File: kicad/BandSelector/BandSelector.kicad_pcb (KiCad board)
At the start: 2 copper layers, 105.5 x 77.6 mm, 60 parts, among them J1 DE15_Plug_HighDensity_Mountin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, J2 POWER, J3 75915416LF, Q1 2N7000, Q2 2N7000, U1 L7805, U2 PicoW

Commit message: better, better.
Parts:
- moved Q2 28.6 mm to (138.6, 72.2), turned to 180 degrees
- moved #G1 25.1 mm to (200.0, 104.8)
- moved TP8 24.5 mm to (148.6, 89.5)
- moved TP9 24.4 mm to (146.1, 89.5)
- moved U2 24.4 mm to (149.9, 103.0)
- moved TP4 24.3 mm to (174.0, 116.8)
- moved TP5 24.3 mm to (128.3, 116.8)
- moved TP3 24.3 mm to (171.4, 116.8)
- moved TP6 24.3 mm to (125.7, 116.8)
- moved TP10 24.3 mm to (141.0, 89.5)
- moved C8 19.5 mm to (132.2, 71.1), turned to -90 degrees
- moved C4 19.4 mm to (122.4, 68.6), turned to -90 degrees
- moved L4 18.6 mm to (128.8, 57.8)
- moved L5 16.5 mm to (139.4, 68.1)
- moved C7 15.6 mm to (125.6, 65.0), turned to 90 degrees
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- renumbered G*** to #G1
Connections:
- net Net-(J1-Pad6) renamed /DIGOUT0
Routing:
- net +3.3V: track 118.8 -> 57.0 mm, vias 1 -> 0
- net Net-(Q1-D): track 0.00 -> 20.1 mm
- net /BAND0: track 22.9 -> 40.0 mm
- net Net-(Q2-G): track 26.9 -> 15.1 mm
- net /BLINKY: track 21.5 -> 32.0 mm
- net /PWRON: track 6.12 -> 16.6 mm
- net /\PWRSENSE: track 8.15 -> 16.8 mm
- net /B3: track 8.59 -> 17.2 mm
- net /\PWR_ON: track 24.5 -> 18.1 mm
- net /B2: track 8.72 -> 13.5 mm
- net Net-(D6-K): track 22.0 -> 26.3 mm
- net Net-(D9-K): track 22.0 -> 17.8 mm
- net /DIGOUT1: track 19.8 -> 16.0 mm
- net +5VD: track 76.7 -> 73.2 mm
- net Net-(D8-K): track 33.5 -> 36.9 mm
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
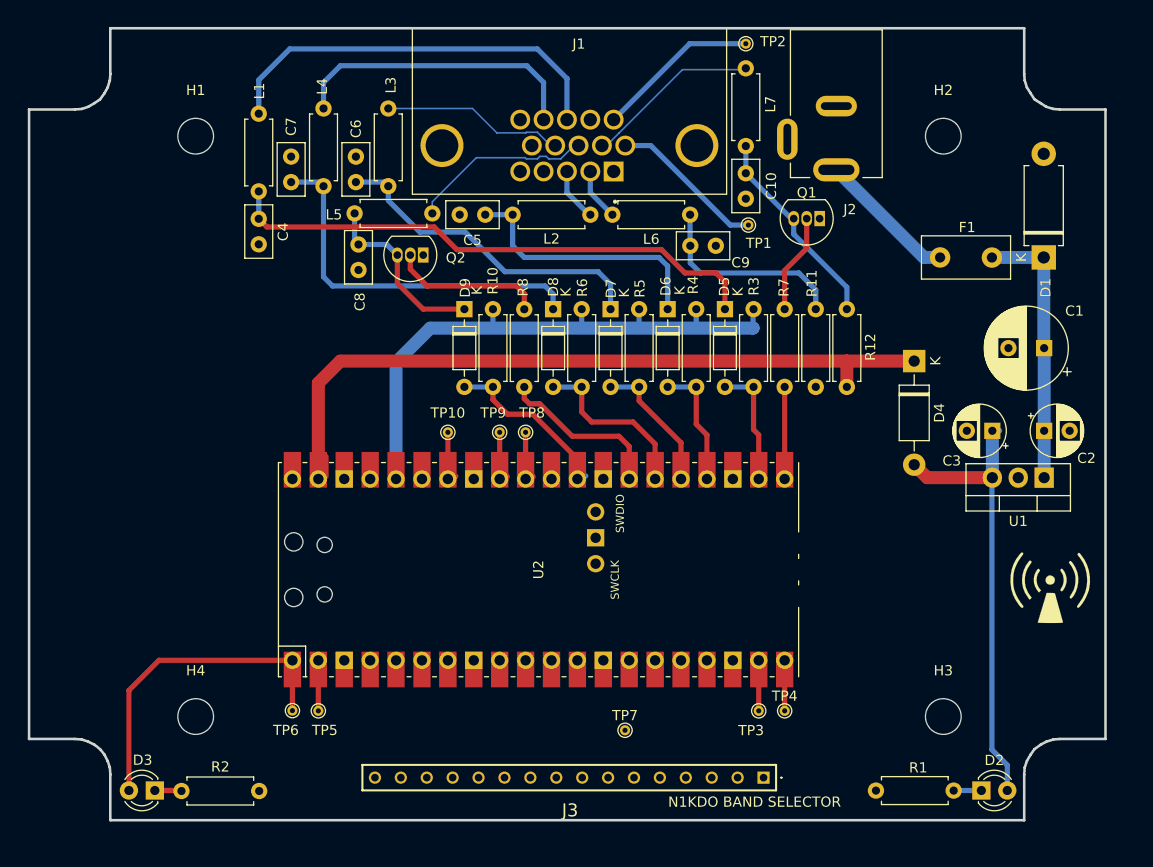
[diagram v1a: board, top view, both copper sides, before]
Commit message: circuit changes.
connector is placed.
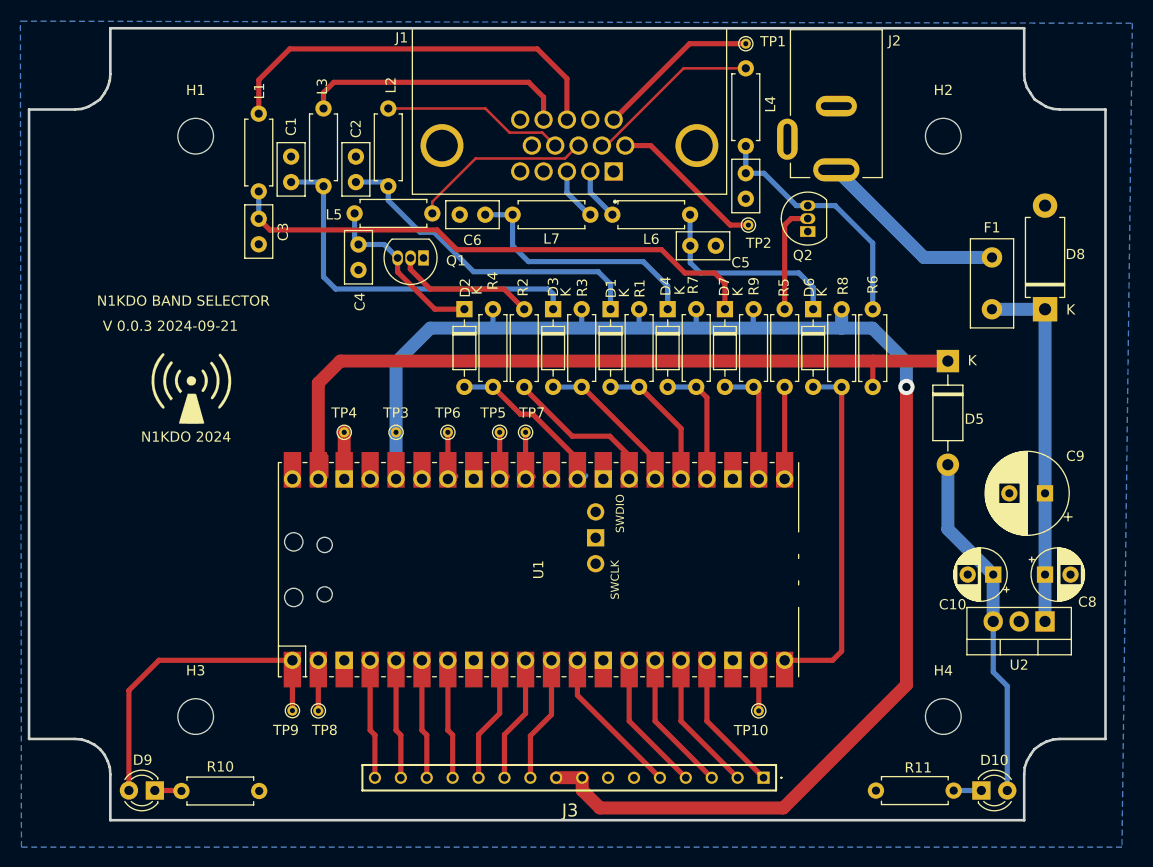
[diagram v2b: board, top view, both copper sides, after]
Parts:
- removed the R11 at (177.0, 77.5)
- removed the TP7 at (158.3, 118.7)
- added D6: BAT43, Diode_THT:D_DO-35_SOD27_P7.62mm_Horizontal, F.Cu at (176.8, 77.5)
- added R8: 10K, Resistor_THT:R_Axial_DIN0207_L6.3mm_D2.5mm_P7.62mm_Horizontal, F.Cu at (179.6, 77.5)
- added TP3: TestPoint, TestPoint:TestPoint_THTPad_D1.0mm_Drill0.5mm, F.Cu at (135.9, 89.5)
- J1: footprint Library:AMPHENOL_10090926-P154XLF -> Library:AMPHENOL_10090926-P154XLF_N1KDO
- moved #G1 86.4 mm to (115.8, 85.2)
- moved TP4 51.1 mm to (130.8, 89.5)
- moved C9 14.2 mm to (199.5, 95.5)
- moved C10 14.1 mm to (194.4, 103.5)
- moved C8 14.1 mm to (199.5, 103.5)
- moved U2 14.1 mm to (199.5, 108.1)
- moved F1 5.09 mm to (194.3, 72.4), turned to -90 degrees
- moved D8 5.08 mm to (199.5, 77.5)
- moved D5 3.30 mm to (190.0, 82.5)
- moved R6 2.54 mm to (182.6, 85.1)
- moved Q2 1.72 mm to (176.3, 69.8), turned to 90 degrees
- moved Q1 0.28 mm to (138.6, 72.4)
- renumbered C7 to C1, C3 to C10, C6 to C2, C4 to C3, C8 to C4, C9 to C5, C5 to C6, C10 to C7, C2 to C8, C1 to C9, D7 to D1, D2 to D10, D9 to D2, D8 to D3, D6 to D4, D4 to D5, D5 to D7, D1 to D8, D3 to D9, H4 to H3, H3 to H4, L3 to L2, L4 to L3, L7 to L4, L2 to L7, Q2 to Q1, Q1 to Q2, R5 to R1, R2 to R10, R1 to R11, R8 to R2, R6 to R3, R10 to R4, R7 to R5, R12 to R6, R4 to R7, R3 to R9, TP2 to TP1, TP3 to TP10, TP1 to TP2, TP9 to TP5, TP10 to TP6, TP8 to TP7, TP5 to TP8, TP6 to TP9, U2 to U1, U1 to U2
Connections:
- J3 pad 5: Net-(J3-Pad5) -> /LIGHT
- TP4 pad 1: Net-(U2-GPIO15) -> GND
- U1 pad 12: /LISTEN -> /LIGHT
- U1 pad 20: Net-(U2-GPIO15) -> /LISTEN
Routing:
- net +3.3V: track 57.0 -> 147.9 mm, vias 0 -> 1
- net /LISTEN: track 0.00 -> 34.7 mm
- net /LIGHT: track 0.00 -> 14.9 mm
- net /SW4: track 0.00 -> 13.8 mm
- net /SW3: track 0.00 -> 13.8 mm
- net /SW2: track 0.00 -> 13.8 mm
- net /SW1: track 0.00 -> 13.8 mm
- net /D4: track 0.00 -> 12.4 mm
- net /E: track 0.00 -> 12.4 mm
- net /RS: track 0.00 -> 12.4 mm
- net /RW: track 0.00 -> 12.4 mm
- net /D6: track 0.00 -> 11.7 mm
- net /D7: track 0.00 -> 11.7 mm
- net /D5: track 0.00 -> 11.7 mm
- net +5V: track 44.2 -> 34.4 mm
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- added copper zone on B.Cu, net GND
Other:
- board text added: "N1KDO 2024"
- board text added: "V 0.0.3 2024-09-21"

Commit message: move auxbus listen to TP configure pushbuttons to send events.
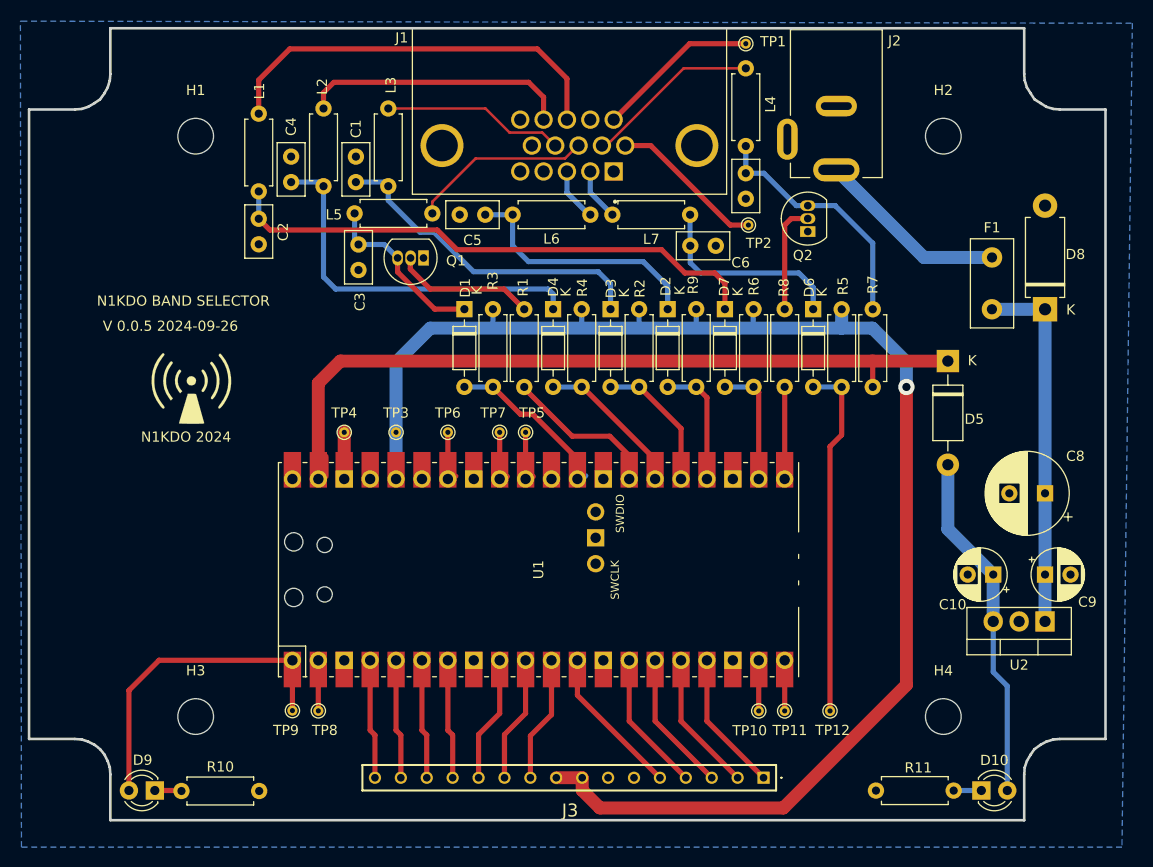
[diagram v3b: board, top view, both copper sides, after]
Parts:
- added TP11: TestPoint, TestPoint:TestPoint_THTPad_D1.0mm_Drill0.5mm, F.Cu at (174.0, 116.8)
- added TP12: TestPoint, TestPoint:TestPoint_THTPad_D1.0mm_Drill0.5mm, F.Cu at (178.4, 116.8)
- renumbered C2 to C1, C3 to C2, C4 to C3, C1 to C4, C6 to C5, C5 to C6, C9 to C8, C8 to C9, D2 to D1, D4 to D2, D1 to D3, D3 to D4, L3 to L2, L2 to L3, L7 to L6, L6 to L7, R2 to R1, R1 to R2, R4 to R3, R3 to R4, R8 to R5, R9 to R6, R6 to R7, R5 to R8, R7 to R9, TP7 to TP5, TP5 to TP7
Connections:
- D6 pad 2: /LISTEN -> Net-(D6-A)
- R5 pad 2: /LISTEN -> Net-(D6-A)
- U1 pad 20: /LISTEN -> Net-(U1-GPIO15)
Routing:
- net Net-(D6-A): track 0.00 -> 35.0 mm
- net /LISTEN: track 34.7 -> 0.00 mm
- net Net-(U1-GPIO15): track 0.00 -> 4.95 mm
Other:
- board text added: "V 0.0.5 2024-09-26"
- board text removed: "V 0.0.3 2024-09-21"

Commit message: software, meet hardware.
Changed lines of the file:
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@@
 			(layers "*.Cu" "*.Mask")
 			(remove_unused_layers no)
-			(net 6 "Net-(D1-K)")
+			(net 11 "Net-(D3-K)")
 			(pinfunction "2")
 			(pintype "passive")
@@
 			(layers "*.Cu" "*.Mask")
 			(remove_unused_layers no)
-			(net 11 "Net-(D3-K)")
+			(net 7 "Net-(D4-K)")
 			(pintype "passive")
 		)
@@
 			(layers "*.Cu" "*.Mask")
 			(remove_unused_layers no)
-			(net 9 "Net-(D2-K)")
+			(net 6 "Net-(D1-K)")
 			(pinfunction "K")
 			(pintype "passive")
@@
 			(layers "*.Cu" "*.Mask")
 			(remove_unused_layers no)
-			(net 9 "Net-(D2-K)")
+			(net 6 "Net-(D1-K)")
 			(pinfunction "D")
 			(pintype "passive")
@@
 			(layers "*.Cu" "*.Mask")
 			(remove_unused_layers no)
-			(net 6 "Net-(D1-K)")
+			(net 11 "Net-(D3-K)")
 			(pintype "passive")
 		)
@@
 			(layers "*.Cu" "*.Mask")
 			(remove_unused_layers no)
-			(net 7 "Net-(D4-K)")
+			(net 9 "Net-(D2-K)")
 			(pinfunction "2")
 			(pintype "passive")
@@
 			(layers "*.Cu" "*.Mask")
 			(remove_unused_layers no)
-			(net 6 "Net-(D1-K)")
+			(net 11 "Net-(D3-K)")
 			(pinfunction "K")
 			(pintype "passive")
@@
 			(layers "*.Cu" "*.Mask")
 			(remove_unused_layers no)
-			(net 9 "Net-(D2-K)")
+			(net 6 "Net-(D1-K)")
 			(pinfunction "2")
 			(pintype "passive")
@@
 			(layers "*.Cu" "*.Mask")
 			(remove_unused_layers no)
-			(net 9 "Net-(D2-K)")
+			(net 6 "Net-(D1-K)")
 			(pintype "passive")
 		)
@@
 			(layers "*.Cu" "*.Mask")
 			(remove_unused_layers no)
-			(net 7 "Net-(D4-K)")
+			(net 9 "Net-(D2-K)")
 			(pintype "passive")
 		)
@@
 			(layers "*.Cu" "*.Mask")
 			(remove_unused_layers no)
-			(net 11 "Net-(D3-K)")
+			(net 7 "Net-(D4-K)")
 			(pinfunction "K")
 			(pintype "passive")
@@
 			(layers "*.Cu" "*.Mask")
 			(remove_unused_layers no)
-			(net 11 "Net-(D3-K)")
+			(net 7 "Net-(D4-K)")
 			(pinfunction "2")
 			(pintype "passive")
@@
 			(layers "*.Cu" "*.Mask")
 			(remove_unused_layers no)
-			(net 7 "Net-(D4-K)")
+			(net 9 "Net-(D2-K)")
 			(pinfunction "K")
 			(pintype "passive")
@@
 	)
 	(segment
-		(start 156.92 77.04)
-		(end 156.92 77.47)
-		(width 0.508)
-		(layer "B.Cu")
-		(net 6)
-	)
-	(segment
-		(start 134.727 65.004)
-		(end 135.128 65.405)
-		(width 0.508)
-		(layer "B.Cu")
-		(net 6)
-	)
-	(segment
-		(start 156.92 75.005)
-		(end 155.702 73.787)
-		(width 0.508)
-		(layer "B.Cu")
-		(net 6)
-	)
-	(segment
-		(start 138.2395 69.9135)
-		(end 135.128 66.802)
+		(start 142.59 77.46)
+		(end 139.69 77.46)
 		(width 0.508)
-		(layer "B.Cu")
+		(layer "F.Cu")
 		(net 6)
 	)
 	(segment
-		(start 156.92 77.46)
-		(end 156.92 75.005)
+		(start 136.0424 73.8124)
+		(end 136.0424 72.4408)
 		(width 0.508)
-		(layer "B.Cu")
+		(layer "F.Cu")
 		(net 6)
 	)
 	(segment
-		(start 135.128 66.802)
-		(end 135.128 65.405)
+		(start 139.69 77.46)
+		(end 136.0424 73.8124)
 		(width 0.508)
-		(layer "B.Cu")
+		(layer "F.Cu")
 		(net 6)
 	)
 	(segment
-		(start 143.4846 73.787)
-		(end 139.6111 69.9135)
+		(start 131.826 70.739)
+		(end 132.207 71.12)
 		(width 0.508)
 		(layer "B.Cu")
@@
 	)
 	(segment
-		(start 131.953 65.004)
-		(end 134.727 65.004)
+		(start 131.826 68.072)
+		(end 131.826 70.739)
 		(width 0.508)
 		(layer "B.Cu")
@@
 	)
 	(segment
-		(start 139.6111 69.9135)
-		(end 138.2395 69.9135)
+		(start 134.7216 71.12)
+		(end 136.0424 72.4408)
 		(width 0.508)
 		(layer "B.Cu")
@@
 	)
 	(segment
-		(start 155.702 73.787)
-		(end 143.4846 73.787)
+		(start 132.207 71.12)
+		(end 134.7216 71.12)
 		(width 0.508)
 		(layer "B.Cu")
@@
 	)
 	(segment
-		(start 147.32 71.247)
-		(end 148.8694 72.7964)
+		(start 128.377 65.004)
+		(end 128.778 65.405)
 		(width 0.508)
 		(layer "B.Cu")
@@
 	)
 	(segment
-		(start 144.633 68.199)
-		(end 147.32 68.199)
+		(start 125.603 65.004)
+		(end 128.377 65.004)
 		(width 0.508)
 		(layer "B.Cu")
@@
 	)
 	(segment
-		(start 162.52 75.1948)
-		(end 162.52 77.46)
+		(start 150.7998 75.4888)
+		(end 129.9718 75.4888)
 		(width 0.508)
 		(layer "B.Cu")
@@
 	)
 	(segment
-		(start 147.32 68.199)
-		(end 147.32 71.247)
+		(start 151.29 75.979)
+		(end 150.7998 75.4888)
 		(width 0.508)
 		(layer "B.Cu")
@@
 	)
 	(segment
-		(start 162.52 77.13)
-		(end 162.52 77.47)
+		(start 128.778 74.295)
+		(end 128.778 65.405)
 		(width 0.508)
 		(layer "B.Cu")
@@
 	)
 	(segment
-		(start 148.8694 72.7964)
-		(end 160.1216 72.7964)
+		(start 129.9718 75.4888)
+		(end 128.778 74.295)
 		(width 0.508)
 		(layer "B.Cu")
@@
 	)
 	(segment
-		(start 160.1216 72.7964)
-		(end 162.52 75.1948)
+		(start 151.29 77.46)
+		(end 151.29 75.979)
 		(width 0.508)
 		(layer "B.Cu")
@@
 	)
 	(segment
-		(start 142.59 77.46)
-		(end 139.69 77.46)
+		(start 147.32 71.247)
+		(end 148.8694 72.7964)
 		(width 0.508)
-		(layer "F.Cu")
+		(layer "B.Cu")
 		(net 9)
 	)
 	(segment
-		(start 136.0424 73.8124)
-		(end 136.0424 72.4408)
+		(start 144.633 68.199)
+		(end 147.32 68.199)
 		(width 0.508)
-		(layer "F.Cu")
+		(layer "B.Cu")
 		(net 9)
 	)
 	(segment
-		(start 139.69 77.46)
-		(end 136.0424 73.8124)
+		(start 162.52 75.1948)
+		(end 162.52 77.46)
 		(width 0.508)
-		(layer "F.Cu")
+		(layer "B.Cu")
 		(net 9)
 	)
 	(segment
-		(start 131.826 70.739)
-		(end 132.207 71.12)
+		(start 147.32 68.199)
+		(end 147.32 71.247)
 		(width 0.508)
 		(layer "B.Cu")
@@
 	)
 	(segment
-		(start 131.826 68.072)
-		(end 131.826 70.739)
+		(start 162.52 77.13)
+		(end 162.52 77.47)
 		(width 0.508)
 		(layer "B.Cu")
@@
 	)
 	(segment
-		(start 134.7216 71.12)
-		(end 136.0424 72.4408)
+		(start 148.8694 72.7964)
+		(end 160.1216 72.7964)
 		(width 0.508)
 		(layer "B.Cu")
@@
 	)
 	(segment
-		(start 132.207 71.12)
-		(end 134.7216 71.12)
+		(start 160.1216 72.7964)
+		(end 162.52 75.1948)
 		(width 0.508)
 		(layer "B.Cu")
@@
 	)
 	(segment
-		(start 128.377 65.004)
-		(end 128.778 65.405)
+		(start 156.92 77.04)
+		(end 156.92 77.47)
 		(width 0.508)
 		(layer "B.Cu")
@@
 	)
 	(segment
-		(start 125.603 65.004)
-		(end 128.377 65.004)
+		(start 134.727 65.004)
+		(end 135.128 65.405)
 		(width 0.508)
 		(layer "B.Cu")
@@
 	)
 	(segment
-		(start 150.7998 75.4888)
-		(end 129.9718 75.4888)
+		(start 156.92 75.005)
+		(end 155.702 73.787)
 		(width 0.508)
 		(layer "B.Cu")
@@
 	)
 	(segment
-		(start 151.29 75.979)
-		(end 150.7998 75.4888)
+		(start 138.2395 69.9135)
+		(end 135.128 66.802)
 		(width 0.508)
 		(layer "B.Cu")
@@
 	)
 	(segment
-		(start 128.778 74.295)
-		(end 128.778 65.405)
+		(start 156.92 77.46)
+		(end 156.92 75.005)
 		(width 0.508)
 		(layer "B.Cu")
@@
 	)
 	(segment
-		(start 129.9718 75.4888)
-		(end 128.778 74.295)
+		(start 135.128 66.802)
+		(end 135.128 65.405)
 		(width 0.508)
 		(layer "B.Cu")
@@
 	)
 	(segment
-		(start 151.29 77.46)
-		(end 151.29 75.979)
+		(start 143.4846 73.787)
+		(end 139.6111 69.9135)
+		(width 0.508)
+		(layer "B.Cu")
+		(net 11)
+	)
+	(segment
+		(start 131.953 65.004)
+		(end 134.727 65.004)
+		(width 0.508)
+		(layer "B.Cu")
+		(net 11)
+	)
+	(segment
+		(start 139.6111 69.9135)
+		(end 138.2395 69.9135)
+		(width 0.508)
+		(layer "B.Cu")
+		(net 11)
+	)
+	(segment
+		(start 155.702 73.787)
+		(end 143.4846 73.787)
 		(width 0.508)
 		(layer "B.Cu")
@@
 		(polygon
 			(pts
-				(xy 99.1616 49.2252) (xy 208.0768 49.4284) (xy 207.0608 130.2004) (xy 99.1616 130.2004) (xy 99.06 49.2252)
+				(xy 99.1616 49.2252) (xy 206.502 49.149) (xy 206.375 128.524) (xy 99.187 128.397) (xy 99.06 49.2252)
 			)
 		)
